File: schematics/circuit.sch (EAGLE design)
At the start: 68 parts, among them IC1 TLC271D, IC2 TLC271D, U1 AD5241BRU1M-REEL7AD5241BRZ1M, X2 87758-0216, X3 87758-0216, X4 87758-0216, X5 87758-0216, X8 87758-0216, X9 87758-0216

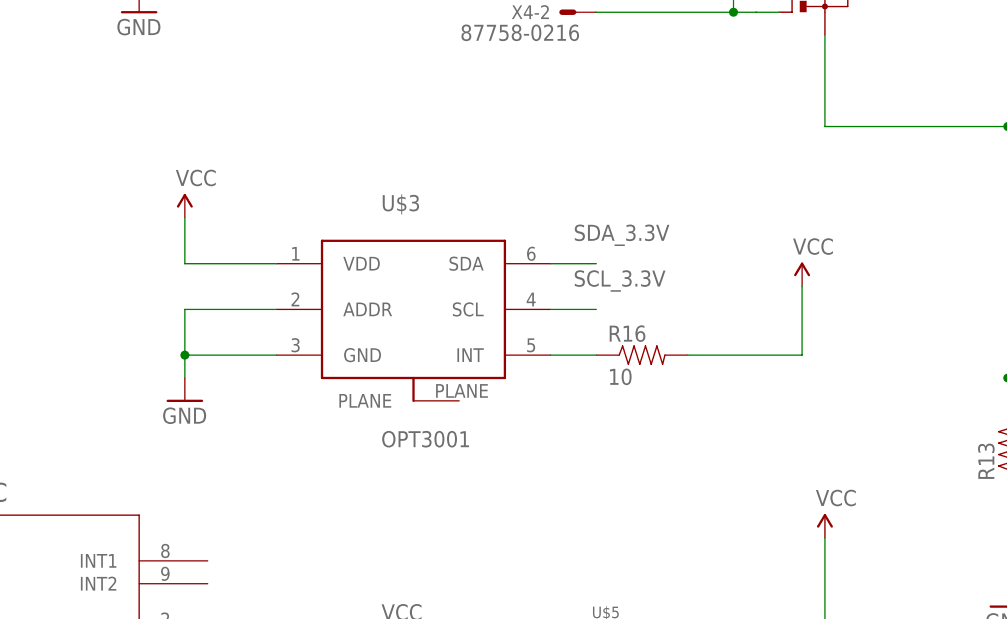
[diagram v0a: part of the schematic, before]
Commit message: Полностью разведена плата
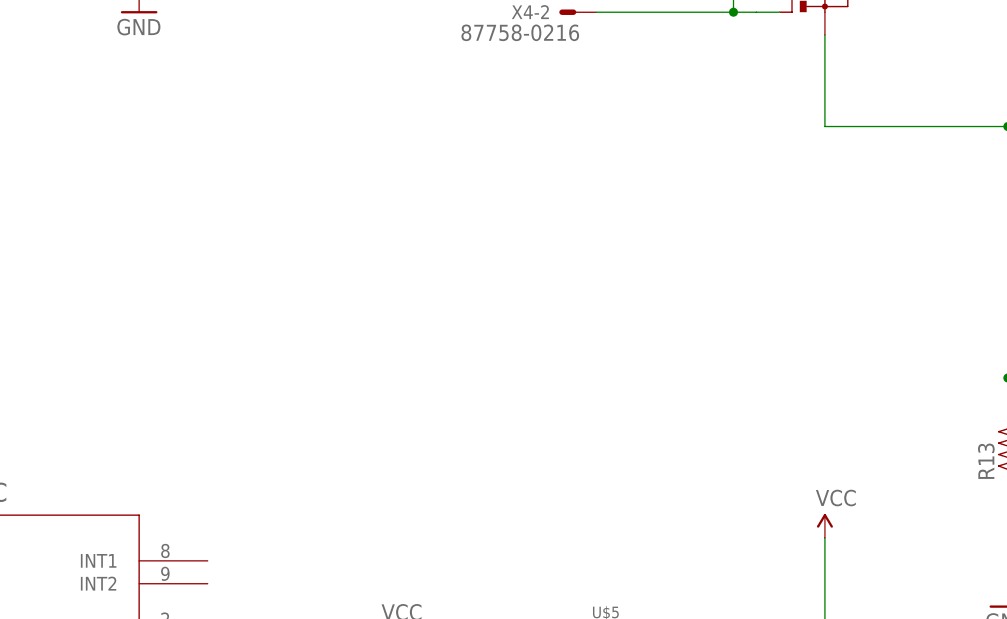
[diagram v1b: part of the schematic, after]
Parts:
- removed R16: 10, SparkFun-Resistors:RESISTOR0402
- removed U$3: OPT3001, datchiki:OPT3001
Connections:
- removed net N$19: R16.1, U$3.INT
- removed net N$25: PROBE_12.P
- net 3.3V: no longer R16.2, U$3.VDD
- net GND: no longer U$3.ADDR, U$3.GND
- net SCL_3.3V: no longer U$3.SCL
- net SDA_3.3V: no longer U$3.SDA
- net VBAT: now also PROBE_12.P
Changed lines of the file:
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@@
 <part name="LED6" library="led" deviceset="LED" device="SML0805"/>
 <part name="GND14" library="SparkFun-Aesthetics" deviceset="GND" device=""/>
-<part name="U$3" library="datchiki" deviceset="OPT3001" device=""/>
-<part name="GND6" library="SparkFun-Aesthetics" deviceset="GND" device=""/>
-<part name="SUPPLY1" library="SparkFun-Aesthetics" deviceset="VCC" device=""/>
-<part name="R16" library="SparkFun-Resistors" deviceset="RESISTOR" device="0402" value="10"/>
 <part name="U$5" library="datchiki" deviceset="TGS4161" device=""/>
 <part name="U$6" library="datchiki" deviceset="O2-A2" device=""/>
@@
 <part name="R19" library="SparkFun-Resistors" deviceset="RESISTOR" device="0402" value="10"/>
 <part name="GND17" library="SparkFun-Aesthetics" deviceset="GND" device=""/>
-<part name="SUPPLY2" library="SparkFun-Aesthetics" deviceset="VCC" device=""/>
 <part name="U$9" library="elements" deviceset="SS-8" device=""/>
 <part name="Q3" library="elements" deviceset="NTR4501N" device=""/>
@@
 <instance part="LED6" gate="G$1" x="342.9" y="71.12" rot="R270"/>
 <instance part="GND14" gate="1" x="330.2" y="68.58"/>
-<instance part="U$3" gate="G$1" x="185.42" y="27.94"/>
-<instance part="GND6" gate="1" x="160.02" y="17.78"/>
-<instance part="SUPPLY1" gate="G$1" x="160.02" y="38.1"/>
-<instance part="R16" gate="G$1" x="210.82" y="22.86"/>
 <instance part="U$5" gate="TGS4161" x="200.66" y="-20.32"/>
 <instance part="U$6" gate="O2-A2" x="101.6" y="50.8"/>
@@
 <instance part="R19" gate="G$1" x="241.3" y="-43.18" rot="R90"/>
 <instance part="GND17" gate="1" x="241.3" y="-53.34"/>
-<instance part="SUPPLY2" gate="G$1" x="228.6" y="30.48"/>
 <instance part="U$9" gate="G$1" x="-33.02" y="66.04"/>
 <instance part="Q3" gate="G$1" x="-55.88" y="-2.54"/>
@@
 <pinref part="SUPPLY6" gate="G$1" pin="VCC"/>
 </segment>
-<segment>
-<pinref part="U$3" gate="G$1" pin="VDD"/>
-<wire x1="170.18" y1="33.02" x2="160.02" y2="33.02" width="0.1524" layer="91"/>
-<wire x1="160.02" y1="33.02" x2="160.02" y2="38.1" width="0.1524" layer="91"/>
-<pinref part="SUPPLY1" gate="G$1" pin="VCC"/>
-</segment>
-<segment>
-<pinref part="R16" gate="G$1" pin="2"/>
-<wire x1="215.9" y1="22.86" x2="228.6" y2="22.86" width="0.1524" layer="91"/>
-<wire x1="228.6" y1="22.86" x2="228.6" y2="30.48" width="0.1524" layer="91"/>
-<pinref part="SUPPLY2" gate="G$1" pin="VCC"/>
-</segment>
 </net>
 <net name="GND" class="0">
@@
 <pinref part="GND14" gate="1" pin="GND"/>
 <wire x1="330.2" y1="71.12" x2="337.82" y2="71.12" width="0.1524" layer="91"/>
-</segment>
-<segment>
-<pinref part="U$3" gate="G$1" pin="GND"/>
-<wire x1="170.18" y1="22.86" x2="160.02" y2="22.86" width="0.1524" layer="91"/>
-<wire x1="160.02" y1="22.86" x2="160.02" y2="20.32" width="0.1524" layer="91"/>
-<pinref part="GND6" gate="1" pin="GND"/>
-<pinref part="U$3" gate="G$1" pin="ADDR"/>
-<wire x1="170.18" y1="27.94" x2="160.02" y2="27.94" width="0.1524" layer="91"/>
-<wire x1="160.02" y1="27.94" x2="160.02" y2="22.86" width="0.1524" layer="91"/>
-<junction x="160.02" y="22.86"/>
 </segment>
 <segment>
@@
 <wire x1="-33.02" y1="60.96" x2="-22.86" y2="60.96" width="0.1524" layer="91"/>
 <junction x="-22.86" y="60.96"/>
-<junction x="-33.02" y="60.96"/>
-<wire x1="-33.02" y1="25.4" x2="-33.02" y2="60.96" width="0.1524" layer="91"/>
+<pinref part="U2" gate="G$1" pin="IN"/>
+<pinref part="U3" gate="G$1" pin="IN"/>
+<pinref part="PROBE_9" gate="P" pin="P"/>
+<wire x1="33.02" y1="25.4" x2="33.02" y2="20.32" width="0.1524" layer="91"/>
+<pinref part="PROBE_6" gate="P" pin="P"/>
+<wire x1="12.7" y1="25.4" x2="12.7" y2="20.32" width="0.1524" layer="91"/>
+<wire x1="12.7" y1="25.4" x2="33.02" y2="25.4" width="0.1524" layer="91"/>
+<junction x="12.7" y="25.4"/>
 <pinref part="PROBE_14" gate="P" pin="P"/>
 <wire x1="-55.88" y1="25.4" x2="-55.88" y2="22.86" width="0.1524" layer="91"/>
 <wire x1="-55.88" y1="25.4" x2="-33.02" y2="25.4" width="0.1524" layer="91"/>
+<wire x1="-33.02" y1="25.4" x2="-10.16" y2="25.4" width="0.1524" layer="91"/>
+<wire x1="-10.16" y1="25.4" x2="12.7" y2="25.4" width="0.1524" layer="91"/>
+<junction x="-10.16" y="25.4"/>
 <wire x1="-10.16" y1="25.4" x2="-10.16" y2="22.86" width="0.1524" layer="91"/>
 <pinref part="PROBE_10" gate="P" pin="P"/>
-<wire x1="-33.02" y1="25.4" x2="-10.16" y2="25.4" width="0.1524" layer="91"/>
+<pinref part="PROBE_12" gate="P" pin="P"/>
+<wire x1="-33.02" y1="25.4" x2="-33.02" y2="22.86" width="0.1524" layer="91"/>
 <junction x="-33.02" y="25.4"/>
-<pinref part="PROBE_6" gate="P" pin="P"/>
-<wire x1="12.7" y1="25.4" x2="12.7" y2="20.32" width="0.1524" layer="91"/>
-<wire x1="-10.16" y1="25.4" x2="12.7" y2="25.4" width="0.1524" layer="91"/>
-<junction x="-10.16" y="25.4"/>
-<wire x1="33.02" y1="25.4" x2="33.02" y2="20.32" width="0.1524" layer="91"/>
-<pinref part="PROBE_9" gate="P" pin="P"/>
-<wire x1="12.7" y1="25.4" x2="33.02" y2="25.4" width="0.1524" layer="91"/>
-<junction x="12.7" y="25.4"/>
-<pinref part="U2" gate="G$1" pin="IN"/>
-<pinref part="U3" gate="G$1" pin="IN"/>
+<wire x1="-33.02" y1="25.4" x2="-33.02" y2="60.96" width="0.1524" layer="91"/>
+<junction x="-33.02" y="60.96"/>
 </segment>
 </net>
@@
 <label x="86.36" y="-17.78" size="1.778" layer="95"/>
 </segment>
-<segment>
-<pinref part="U$3" gate="G$1" pin="SDA"/>
-<wire x1="200.66" y1="33.02" x2="205.74" y2="33.02" width="0.1524" layer="91"/>
-<label x="203.2" y="35.56" size="1.778" layer="95"/>
-</segment>
 </net>
 <net name="SCL_3.3V" class="0">
@@
 <wire x1="106.68" y1="-10.16" x2="81.28" y2="-10.16" width="0.1524" layer="91"/>
 <label x="86.36" y="-7.62" size="1.778" layer="95"/>
-</segment>
-<segment>
-<pinref part="U$3" gate="G$1" pin="SCL"/>
-<wire x1="200.66" y1="27.94" x2="205.74" y2="27.94" width="0.1524" layer="91"/>
-<label x="203.2" y="30.48" size="1.778" layer="95"/>
 </segment>
 </net>
@@
 </segment>
 </net>
-<net name="N$19" class="0">
-<segment>
-<pinref part="U$3" gate="G$1" pin="INT"/>
-<wire x1="200.66" y1="22.86" x2="205.74" y2="22.86" width="0.1524" layer="91"/>
-<pinref part="R16" gate="G$1" pin="1"/>
-</segment>
-</net>
 <net name="N$22" class="0">
 <segment>
@@
 </segment>
 </net>
-<net name="N$25" class="0">
-<segment>
-<wire x1="-33.02" y1="25.4" x2="-33.02" y2="22.86" width="0.1524" layer="91"/>
-<pinref part="PROBE_12" gate="P" pin="P"/>
-</segment>
-</net>

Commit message: Последняя версия платы и схемы
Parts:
- added IC3: TLC271D, linear:TLC271D
- added R10: (no value), SparkFun-Passives:RESISTOR0402-RES
- added R16: (no value), SparkFun-Resistors:RESISTOR0402
- added U4: AD5241BRU1M-REEL7AD5241BRZ1M, elements:AD5241BRU1M-REEL7AD5241BRZ1M
- added X1, X6: 87758-0216, con-molex:87758-0216
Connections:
- removed net N$5: IC2.+IN, R13.2, U$1Q2.S, U$2Q2.S, U$4Q2.S
- new net N$19: R13.2, U4.O1, U4.SHDN*
- new net N$25: IC3.OUT, U4.A1, X6-1.S
- new net N$31: IC2.+IN
- new net N$32: IC3.-IN, R10.1, U4.W1, X1-1.S
- new net VCC: IC3.+IN, IC3.ON1, IC3.OPT, R16.2, U$1Q2.S, U$2Q2.S, U$4Q2.S, U4.AD0, U4.AD1, U4.VDD, U4.VSS, X1-2.S
- net GND: now also IC3.V-, R10.2, R16.1, U4.B1, U4.DGND
- net SCL_5V: now also U4.SCL
- net SDA_5V: now also U4.SDA
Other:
- moved on the sheet: LED1, LED2, LED3, LED4, LED5, LED6, PROBE_1, PROBE_2, PROBE_3, R11, R12, R13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

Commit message: Переделана схема подключения стержней, в библиотеку добавлен MC74HC4051A, к датчику кислорода подключен операционный усилитель
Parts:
- removed IC3: TLC271D, linear:TLC271D
- removed PROBE_1, PROBE_2, PROBE_3: (no value), wirepad:2,54/0,8
- removed R12: 10, SparkFun-Resistors:RESISTOR0402
- removed R13, R14, R17: (no value), SparkFun-Passives:RESISTOR0402-RES
- removed R16: (no value), SparkFun-Resistors:RESISTOR0402
- removed U$6: O2-A2, datchiki:O2-A2
- removed U4: AD5241BRU1M-REEL7AD5241BRZ1M, elements:AD5241BRU1M-REEL7AD5241BRZ1M
- removed X4, X5, X9: 87758-0216, con-molex:87758-0216
- added GROUND_PROBE1, GROUND_PROBE2, GROUND_PROBE3, PROBE_15: (no value), wirepad:2,54/0,8
- added U$3: MC74HC4051A, elements:MC74HC4051A
- added X10, X7: 87758-0216, con-molex:87758-0216
- R10: value (none) -> 10; device SparkFun-Passives:RESISTOR0402-RES -> SparkFun-Resistors:RESISTOR0402
- R11, R5, R6, R7: value 10 -> 10k; device SparkFun-Resistors:RESISTOR0402 -> SparkFun-Passives:RESISTOR0402-RES
- U$1, U$2: value AO4606 -> MC74HC4051A; device elements:AO4606 -> elements:MC74HC4051A
- U$4: value AO4606 -> O2-A2; device elements:AO4606 -> datchiki:O2-A2
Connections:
- removed net N$17: R6.2, U$1Q2.G, X9-2.S
- removed net N$20: IC2.OUT, U1.A1, X3-1.S
- removed net N$21: PROBE_3.P, U$2Q1.D, U$2Q2.D
- removed net N$25: IC3.OUT, U4.A1, X6-1.S
- removed net N$26: IC2.-IN, U1.W1
- removed net N$28: R14.2, U1.O1, U1.SHDN*
- removed net N$31: IC2.+IN
- removed net N$32: IC3.-IN, R10.1, U4.W1, X1-1.S
- removed net N$7: R12.2, U$4Q1.G, X4-1.S
- new net N$15: U$1.ENABLE, X1-2.S
- new net N$5: GROUND_PROBE2.P, U$3.X
- net 5V: now also IC2.+IN, R5.1, U$1.VCC, U$1.X1, U$2.VCC, U$2.X1, U$3.VCC, U$3.X1, U$4.VOUT, U1.B1; no longer IC2.ON1, IC2.OPT, R17.2, U$1Q1.S, U$2Q1.S, U$4Q1.S, U$6.VOUT, U1.AD0, U1.AD1, U1.VDD, U1.VSS
- net GND: now also R10.1, R11.1, R5.2, R6.1, R7.1, U$4.GND; no longer IC3.V-, LED1.C, LED2.C, LED3.C, LED4.C, LED5.C, LED6.C, R10.2, R13.1, R14.1, R16.1, R17.1, U$6.GND, U4.B1, U4.DGND
- net N$1: now also PROBE_15.P, U$1.GND, U$2.GND, U$3.GND; no longer LED4.A, R12.1
- net N$10: now also IC2.-IN, R10.2, R9.1; no longer LED3.A, R6.1
- net N$11: now also U$3.ENABLE, X7-1.S; no longer R5.2, U$1Q1.G, X9-1.S
- net N$12: now also U$3.A, X7-2.S; no longer LED5.A, R7.1
- net N$13: now also U$2.A, X6-2.S; no longer R7.2, U$2Q1.G, X5-1.S
- net N$14: now also U$1.A, X1-1.S; no longer LED6.A, R9.1
- net N$16: now also U$2.ENABLE, X6-1.S; no longer PROBE_1.P, U$4Q1.D, U$4Q2.D
- net N$19: now also R11.2, U1.O1, U1.SHDN*; no longer R13.2, U4.O1, U4.SHDN*
- net N$2: now also GROUND_PROBE3.P, U$1.X; no longer PROBE_2.P, U$1Q1.D, U$1Q2.D
- net N$4: now also IC2.OUT, R9.2, X10-1.S; no longer LED1.A, R11.1
- net N$6: now also GROUND_PROBE1.P, U$2.X; no longer R11.2, U$4Q2.G, X4-2.S
- net N$8: now also R7.2, U1.W1; no longer LED2.A, R5.1
- net N$9: now also R6.2, U$1.X0, U$2.X0, U$3.X0; no longer R9.2, U$2Q2.G, X5-2.S
- net SCL_3.3V: now also U1.SCL
- net SCL_5V: no longer U1.SCL, U4.SCL
- net SDA_3.3V: now also U1.SDA
- net SDA_5V: no longer U1.SDA, U4.SDA
- net VCC: now also U1.AD0, U1.AD1, U1.VDD, U1.VSS; no longer IC3.+IN, IC3.ON1, IC3.OPT, R16.2, U$1Q2.S, U$2Q2.S, U$4Q2.S, U4.AD0, U4.AD1, U4.VDD, U4.VSS, X1-2.S
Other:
- moved on the sheet: HMDT, IC2, LED1, LED2, LED3, LED4, LED5, LED6, R10, R11, R5, R6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

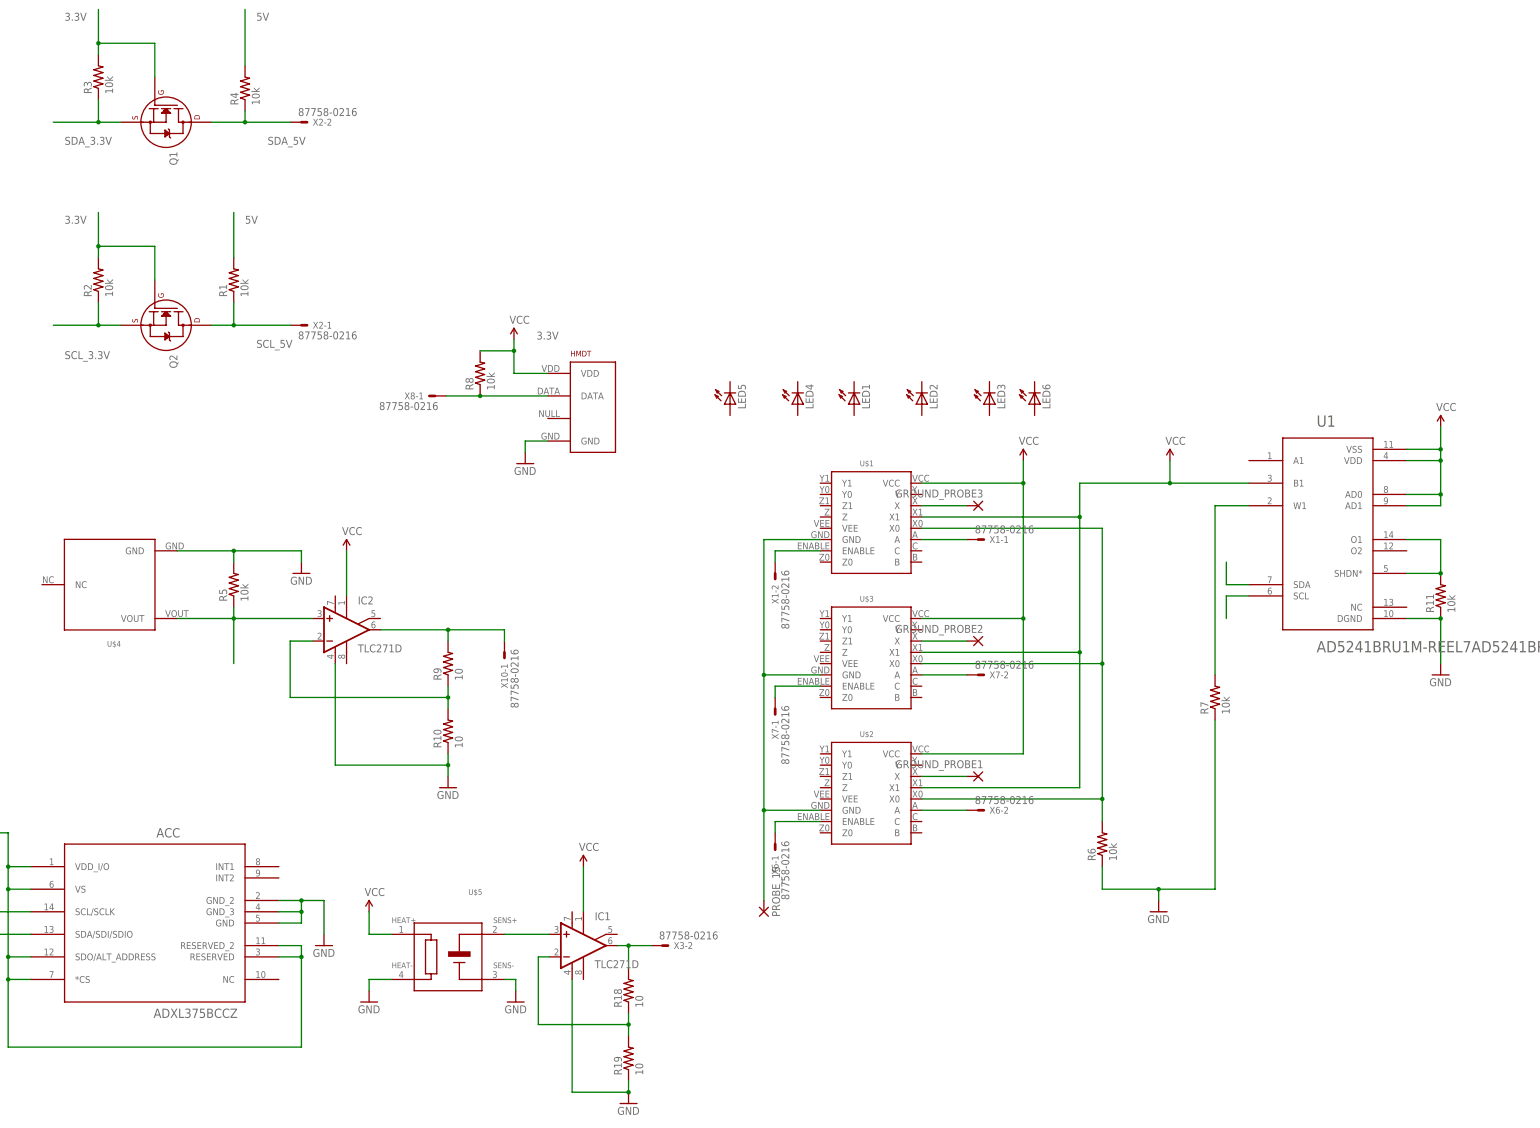
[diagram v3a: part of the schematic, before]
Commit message: Полностью исправлена основная плата (заменены резисторы, изменен диаметр сквозных отверстий, добавлены новые элементы из схемы)
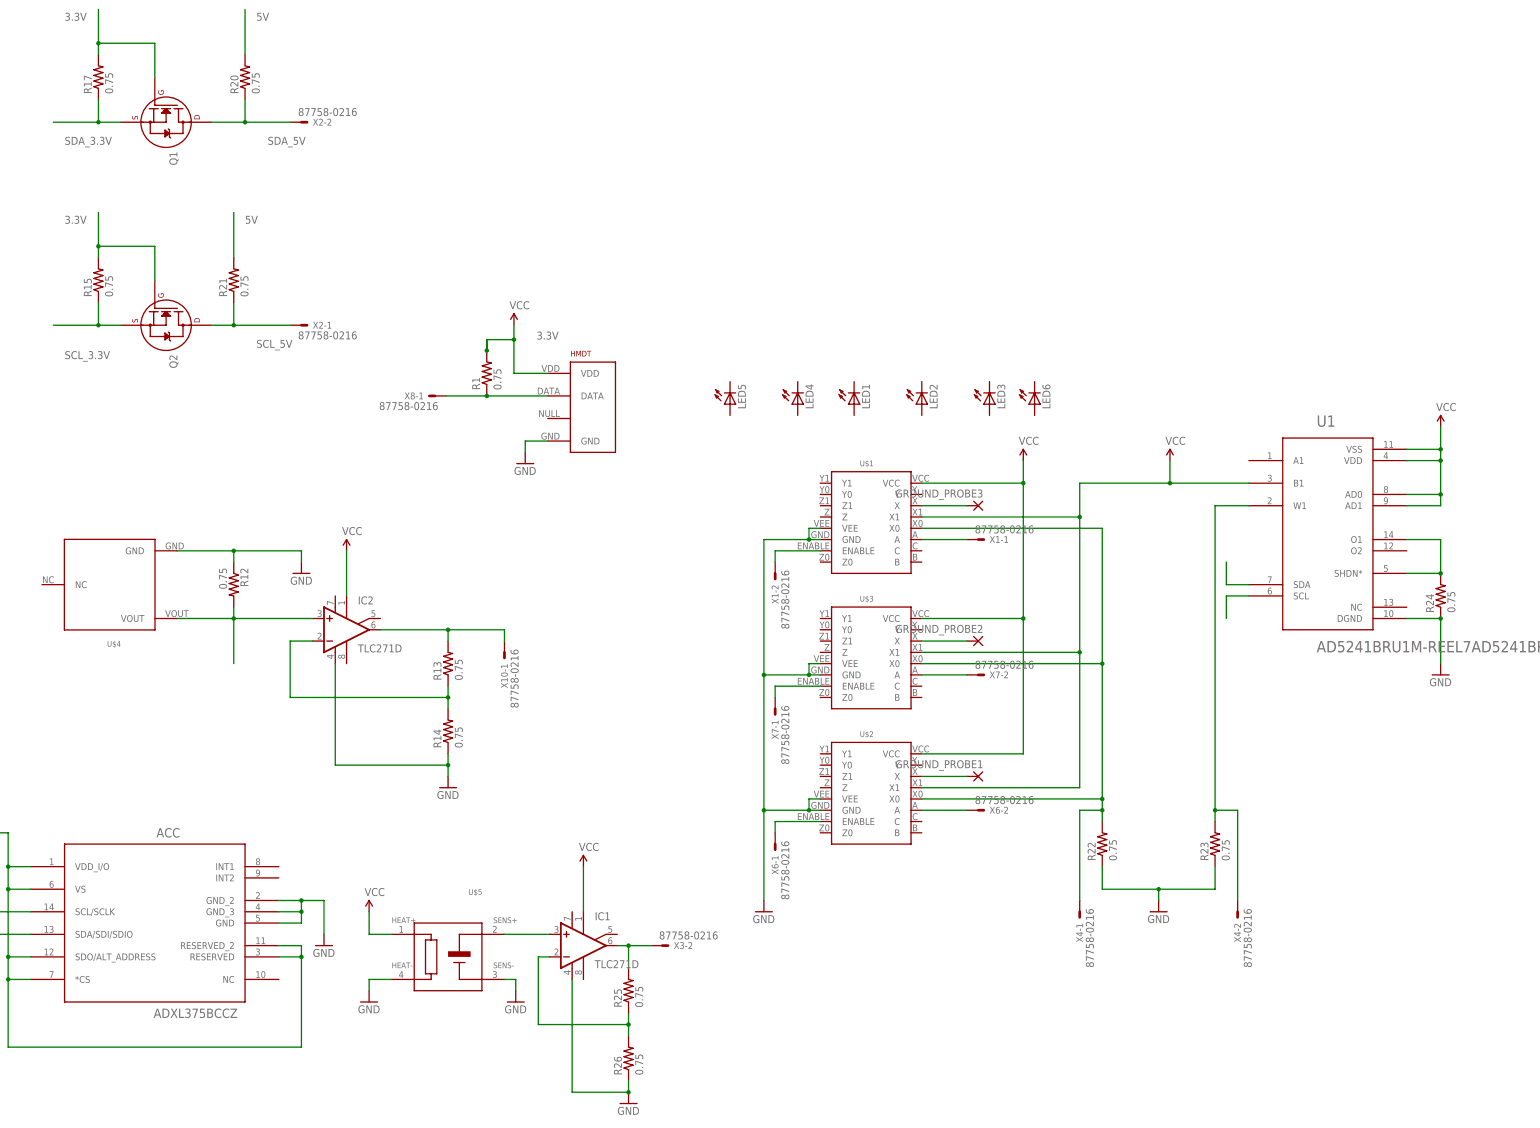
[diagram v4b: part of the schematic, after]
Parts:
- removed PROBE_15: (no value), wirepad:2,54/0,8
- removed R10, R18, R19, R9: 10, SparkFun-Resistors:RESISTOR0402
- removed R11, R2, R3, R4, R5, R6, R7, R8: 10k, SparkFun-Passives:RESISTOR0402-RES
- added R12, R13, R14, R15, R17, R20, R21, R22, R23, R24, R25, R26: 0.75, SparkFun-Resistors:0.75OHM-1/4W-1%(0805)
- added X4: 87758-0216, con-molex:87758-0216
- R1: value 10k -> 0.75; device SparkFun-Passives:RESISTOR0402-RES -> SparkFun-Resistors:0.75OHM-1/4W-1%(0805)
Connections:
- removed net N$1: PROBE_15.P, U$1.GND, U$2.GND, U$3.GND
- removed net N$3: HMDT.DATA, R8.1, X8-1.S
- removed net VCC: U1.AD0, U1.AD1, U1.VDD, U1.VSS
- new net N$55: HMDT.DATA, R1.1, X8-1.S
- net 3.3V: now also R1.2, R15.2, R17.2; no longer R2.2, R3.2, R8.2
- net 5V: now also R12.2, R20.2, R21.2, R25.1, R26.2, U1.AD0, U1.AD1, U1.VDD, U1.VSS; no longer R1.2, R18.1, R19.2, R4.2, R5.1
- net GND: now also R12.1, R14.1, R22.1, R23.1, R24.1, R26.1, U$1.GND, U$1.VEE, U$2.GND, U$2.VEE, U$3.GND, U$3.VEE; no longer R10.1, R11.1, R19.1, R5.2, R6.1, R7.1
- net N$10: now also R13.1, R14.2; no longer R10.2, R9.1
- net N$19: now also R24.2; no longer R11.2
- net N$24: now also R25.2; no longer R18.2
- net N$4: now also R13.2; no longer R9.2
- net N$8: now also R23.2, X4-2.S; no longer R7.2
- net N$9: now also R22.2, X4-1.S; no longer R6.2
- net SCL_3.3V: now also R15.1; no longer R2.1
- net SCL_5V: now also R21.1; no longer R1.1
- net SDA_3.3V: now also R17.1; no longer R3.1
- net SDA_5V: now also R20.1; no longer R4.1
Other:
- moved on the sheet: R1
